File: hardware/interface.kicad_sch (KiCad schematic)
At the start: 19 parts

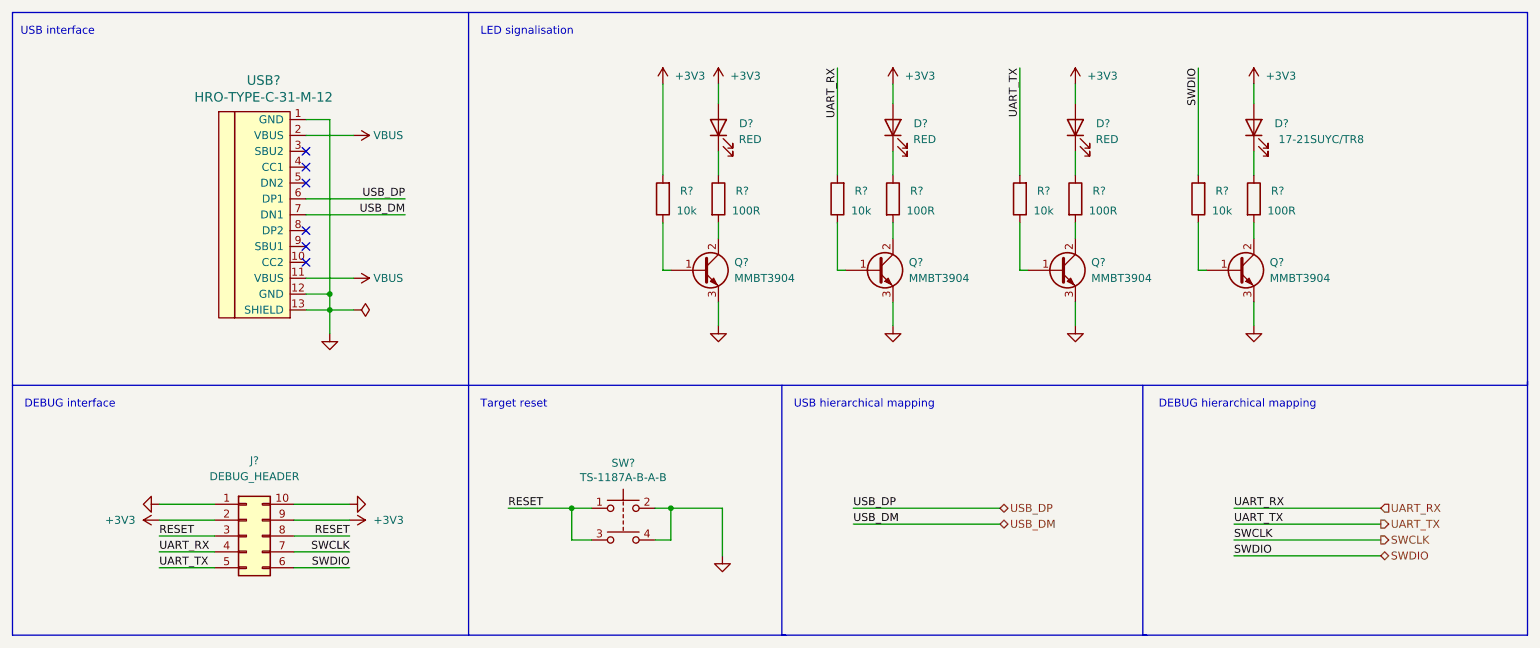
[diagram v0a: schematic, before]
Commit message: hw: Add annotations to all components
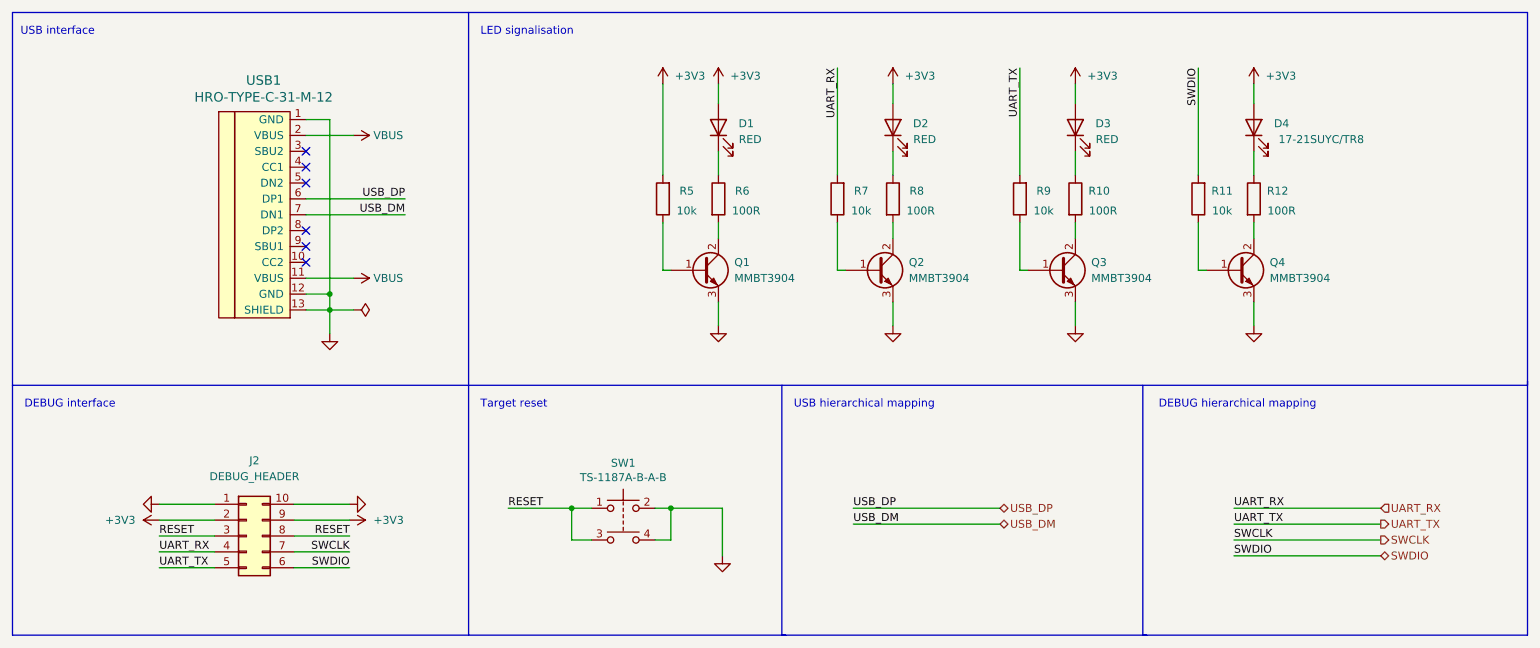
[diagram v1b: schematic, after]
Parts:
- USB1: renamed from USB?; footprint Type-C:HRO-TYPE-C-31-M-12-HandSoldering -> TYPE-C:HRO-TYPE-C-31-M-12-HandSoldering
- gave numbers to parts that had none: 18
